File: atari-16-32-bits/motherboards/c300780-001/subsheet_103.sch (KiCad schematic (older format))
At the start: 0 parts

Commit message: sheet 1 done
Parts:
- added C109: 0.1uF, symbol Device:C
- added C110: 100uF, symbol Device:CP1
- added J103: Cartridge port, symbol Connector:Conn_01x40_Female
- added L100: FB, symbol Device:Ferrite_Bead_Small
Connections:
- new net A1: J103.36 (Pin_36)
- new net A10: J103.26 (Pin_26)
- new net A11: J103.29 (Pin_29)
- new net A12: J103.28 (Pin_28)
- new net A13: J103.19 (Pin_19)
- new net A14: J103.22 (Pin_22)
- new net A15: J103.20 (Pin_20)
- new net A2: J103.34 (Pin_34)
- new net A3: J103.32 (Pin_32)
- new net A4: J103.30 (Pin_30)
- new net A5: J103.27 (Pin_27)
- new net A6: J103.25 (Pin_25)
- new net A7: J103.23 (Pin_23)
- new net A8: J103.21 (Pin_21)
- new net A9: J103.24 (Pin_24)
- new net D0: J103.17 (Pin_17)
- new net D1: J103.18 (Pin_18)
- new net D10: J103.7 (Pin_7)
- new net D11: J103.8 (Pin_8)
- new net D12: J103.5 (Pin_5)
- new net D13: J103.6 (Pin_6)
- new net D14: J103.3 (Pin_3)
- new net D15: J103.4 (Pin_4)
- new net D2: J103.15 (Pin_15)
- new net D3: J103.16 (Pin_16)
- new net D4: J103.13 (Pin_13)
- new net D5: J103.14 (Pin_14)
- new net D6: J103.11 (Pin_11)
- new net D7: J103.12 (Pin_12)
- new net D8: J103.9 (Pin_9)
- new net D9: J103.10 (Pin_10)
- new net FVCC: C109.1, C110.1, J103.1 (Pin_1), J103.2 (Pin_2), L100.2
- new net GND: C109.2, C110.2, J103.38 (Pin_38), J103.39 (Pin_39), J103.40 (Pin_40)
- new net VCC: L100.1
- new net XLDS: J103.37 (Pin_37)
- new net XROM3: J103.31 (Pin_31)
- new net XROM4: J103.33 (Pin_33)
- new net XUDS: J103.35 (Pin_35)

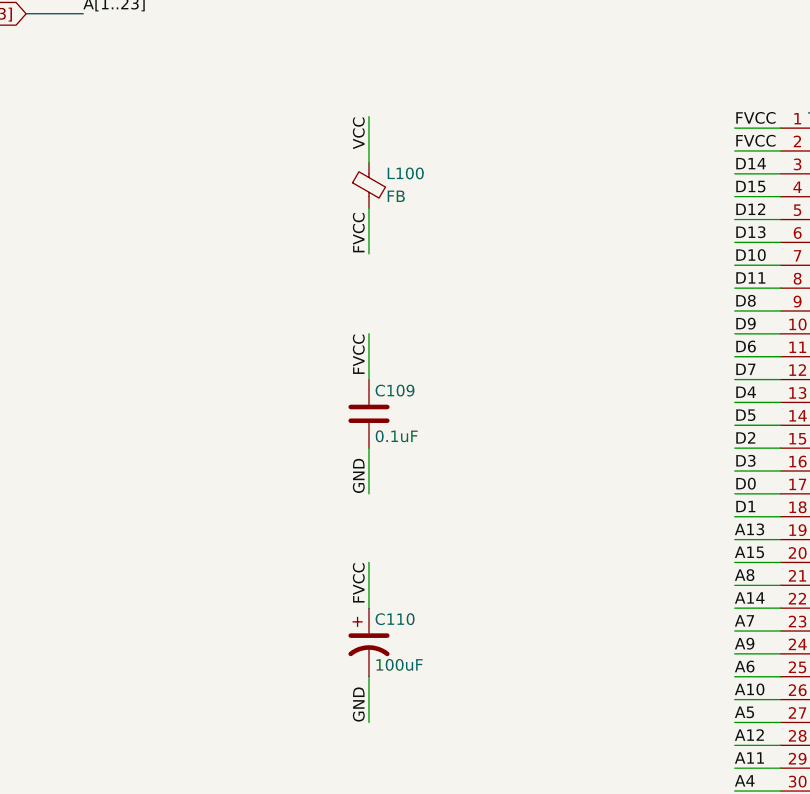
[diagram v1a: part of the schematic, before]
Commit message: reorganized sheets
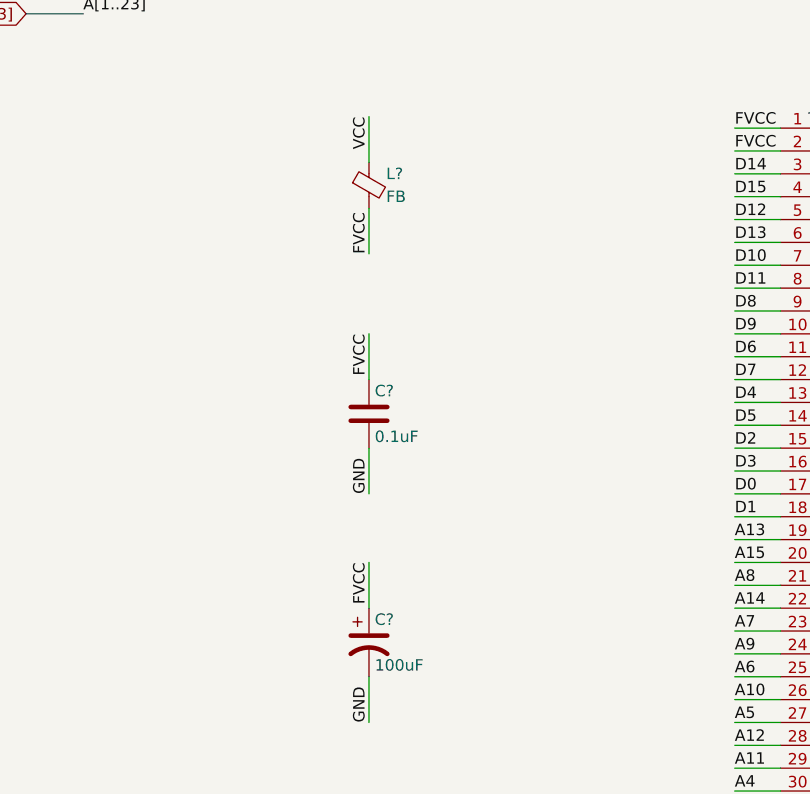
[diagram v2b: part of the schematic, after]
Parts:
- renumbered C109 to C?, C110 to C?, L100 to L?
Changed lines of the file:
@@
 $Descr A4 8268 11693 portrait
 encoding utf-8
-Sheet 6 14
+Sheet 10 8
 Title ""
 Date ""
@@
 	4600 5400 4800 5400
 $Comp
-L Device:Ferrite_Bead_Small L100
+L Device:Ferrite_Bead_Small L?
 U 1 1 6085902E
 P 3000 1750
-F 0 "L100" H 3075 1800 50  0000 L CNN
+F 0 "L?" H 3075 1800 50  0000 L CNN
 F 1 "FB" H 3075 1700 50  0000 L CNN
 F 2 "" V 2930 1750 50  0001 C CNN
@@
 FVCC
 $Comp
-L Device:C C109
+L Device:C C?
 U 1 1 60859F20
 P 3000 2750
-F 0 "C109" H 3025 2850 50  0000 L CNN
+F 0 "C?" H 3025 2850 50  0000 L CNN
 F 1 "0.1uF" H 3025 2650 50  0000 L CNN
 F 2 "" H 3038 2600 50  0001 C CNN
@@
 GND
 $Comp
-L Device:CP1 C110
+L Device:CP1 C?
 U 1 1 6085AF1D
 P 3000 3750
-F 0 "C110" H 3025 3850 50  0000 L CNN
+F 0 "C?" H 3025 3850 50  0000 L CNN
 F 1 "100uF" H 3025 3650 50  0000 L CNN
 F 2 "" H 3000 3750 50  0001 C CNN

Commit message: re-annotate component following move of subsheets in schematics
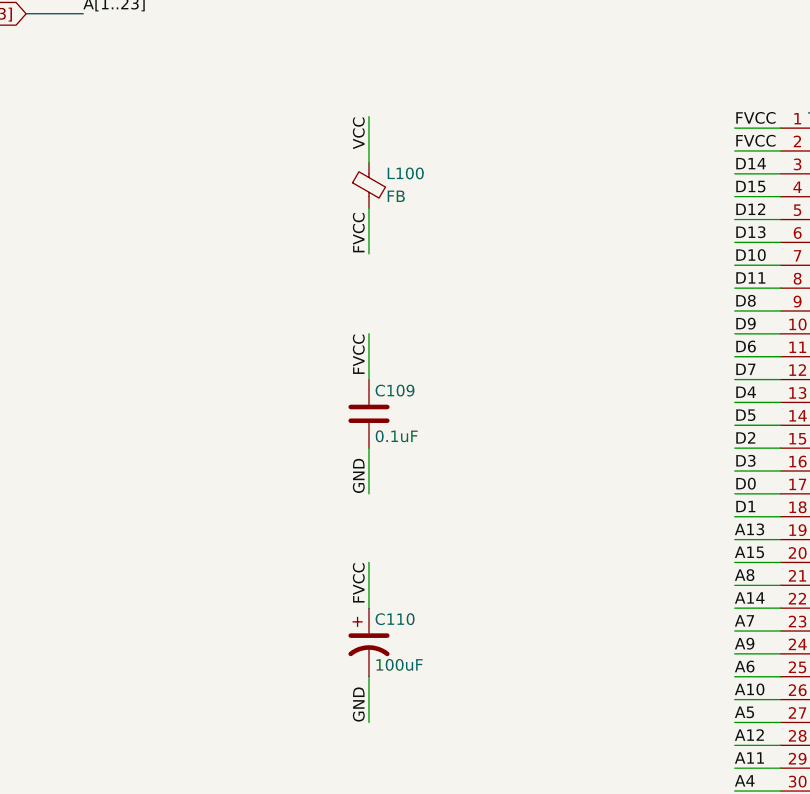
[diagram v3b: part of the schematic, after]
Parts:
- gave numbers to parts that had none: 3
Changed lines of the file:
@@
 $Descr A4 8268 11693 portrait
 encoding utf-8
-Sheet 10 8
+Sheet 4 9
 Title ""
 Date ""
@@
 	4600 5400 4800 5400
 $Comp
-L Device:Ferrite_Bead_Small L?
+L Device:Ferrite_Bead_Small L100
 U 1 1 6085902E
 P 3000 1750
-F 0 "L?" H 3075 1800 50  0000 L CNN
+F 0 "L100" H 3075 1800 50  0000 L CNN
 F 1 "FB" H 3075 1700 50  0000 L CNN
 F 2 "" V 2930 1750 50  0001 C CNN
@@
 FVCC
 $Comp
-L Device:C C?
+L Device:C C109
 U 1 1 60859F20
 P 3000 2750
-F 0 "C?" H 3025 2850 50  0000 L CNN
+F 0 "C109" H 3025 2850 50  0000 L CNN
 F 1 "0.1uF" H 3025 2650 50  0000 L CNN
 F 2 "" H 3038 2600 50  0001 C CNN
@@
 GND
 $Comp
-L Device:CP1 C?
+L Device:CP1 C110
 U 1 1 6085AF1D
 P 3000 3750
-F 0 "C?" H 3025 3850 50  0000 L CNN
+F 0 "C110" H 3025 3850 50  0000 L CNN
 F 1 "100uF" H 3025 3650 50  0000 L CNN
 F 2 "" H 3000 3750 50  0001 C CNN
